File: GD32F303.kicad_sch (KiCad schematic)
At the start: 0 parts

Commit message: 更新原理图
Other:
- sheet MCU_Core ports: added CAN_RX, CAN_TX, RS232_RX, RS232_TX, RS485_DE, RS485_RX, RS485_TX, USB_DM, USB_DP; removed none
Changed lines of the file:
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@@
 	(paper "A3")
 	(sheet
-		(at 272.415 133.985)
-		(size 26.035 13.335)
+		(at 196.977 137.922)
+		(size 24.765 13.335)
 		(exclude_from_sim no)
 		(in_bom yes)
@@
 		)
 		(property "Sheetname" "RS485"
-			(at 272.415 133.2734 0)
+			(at 196.977 137.2104 0)
 			(show_name no)
 			(do_not_autoplace no)
@@
 		)
 		(property "Sheetfile" "RS485.kicad_sch"
-			(at 272.415 147.9046 0)
+			(at 196.977 151.8416 0)
 			(show_name no)
 			(do_not_autoplace no)
@@
 	)
 	(sheet
-		(at 273.05 90.805)
-		(size 28.575 15.875)
+		(at 197.612 96.012)
+		(size 24.13 14.605)
 		(exclude_from_sim no)
 		(in_bom yes)
@@
 		)
 		(property "Sheetname" "CAN"
-			(at 273.05 90.0934 0)
+			(at 197.612 95.3004 0)
 			(show_name no)
 			(do_not_autoplace no)
@@
 		)
 		(property "Sheetfile" "CAN.kicad_sch"
-			(at 273.05 107.2646 0)
+			(at 197.612 111.2016 0)
 			(show_name no)
 			(do_not_autoplace no)
@@
 	)
 	(sheet
-		(at 273.05 114.3)
+		(at 197.612 118.237)
 		(size 24.13 14.605)
 		(exclude_from_sim no)
@@
 		)
 		(property "Sheetname" "RS232"
-			(at 273.05 113.5884 0)
+			(at 197.612 117.5254 0)
 			(show_name no)
 			(do_not_autoplace no)
@@
 		)
 		(property "Sheetfile" "RS232.kicad_sch"
-			(at 273.05 129.4896 0)
+			(at 197.612 133.4266 0)
 			(show_name no)
 			(do_not_autoplace no)
@@
 	)
 	(sheet
-		(at 149.86 91.059)
-		(size 30.48 36.576)
+		(at 139.7 21.844)
+		(size 114.935 36.576)
 		(exclude_from_sim no)
 		(in_bom yes)
@@
 		)
 		(property "Sheetname" "POWER"
-			(at 149.86 90.3474 0)
+			(at 139.7 21.1324 0)
 			(show_name no)
 			(do_not_autoplace no)
@@
 		)
 		(property "Sheetfile" "POWER.kicad_sch"
-			(at 149.86 128.2196 0)
+			(at 139.7 59.0046 0)
 			(show_name no)
 			(do_not_autoplace no)
@@
 	)
 	(sheet
-		(at 203.708 90.043)
+		(at 128.27 93.98)
 		(size 35.306 53.086)
 		(exclude_from_sim no)
@@
 		)
 		(property "Sheetname" "MCU_Core"
-			(at 203.708 89.3314 0)
+			(at 128.27 93.2684 0)
 			(show_name no)
 			(do_not_autoplace no)
@@
 		)
 		(property "Sheetfile" "STM32F303VCT6.kicad_sch"
-			(at 203.708 143.7136 0)
-			(show_name no)
-			(do_not_autoplace no)
-			(effects
-				(font
-					(size 1.27 1.27)
-				)
-				(justify left top)
-			)
-		)
+			(at 128.27 147.6506 0)
+			(show_name no)
+			(do_not_autoplace no)
+			(effects
+				(font
+					(size 1.27 1.27)
+				)
+				(justify left top)
+			)
+		)
+		(pin "CAN_RX" input
+			(at 163.576 100.33 0)
+			(effects
+				(font
+					(size 1.27 1.27)
+				)
+				(justify right)
+			)
+		)
+		(pin "RS232_RX" input
+			(at 163.576 128.27 0)
+			(effects
+				(font
+					(size 1.27 1.27)
+				)
+				(justify right)
+			)
+		)
+		(pin "CAN_TX" output
+			(at 163.576 104.14 0)
+			(effects
+				(font
+					(size 1.27 1.27)
+				)
+				(justify right)
+			)
+		)
+		(pin "RS232_TX" output
+			(at 163.576 124.46 0)
+			(effects
+				(font
+					(size 1.27 1.27)
+				)
+				(justify right)
+			)
+		)
+		(pin "RS485_RX" bidirectional
+			(at 163.576 142.24 0)
+			(effects
+				(font
+					(size 1.27 1.27)
+				)
+				(justify right)
+			)
+		)
+		(pin "RS485_TX" bidirectional
+			(at 163.576 139.7 0)
+			(effects
+				(font
+					(size 1.27 1.27)
+				)
+				(justify right)
+			)
+		)
+		(pin "RS485_DE" output
+			(at 163.576 137.16 0)
+			(effects
+				(font
+					(size 1.27 1.27)
+				)
+				(justify right)
+			)
+		)
+		(pin "USB_DP" bidirectional
+			(at 128.27 107.95 180)
+			(effects
+				(font
+					(size 1.27 1.27)
+				)
+				(justify left)
+			)
+		)
+		(pin "USB_DM" bidirectional
+			(at 128.27 111.76 180)
+			(effects
+				(font
+					(size 1.27 1.27)
+				)
+				(justify left)
+			)
+		)

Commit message: 增加USB,TYPEC转串口esd隔离，
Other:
- sheet MCU_Core ports: added MCU_RS232_RX, MCU_RS232_TX; removed RS232_RX, RS232_TX
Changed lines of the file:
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@@
 			)
 		)
-		(pin "RS232_RX" input
+		(pin "MCU_RS232_RX" input
 			(at 163.576 128.27 0)
 			(effects
@@
 			)
 		)
-		(pin "RS232_TX" output
+		(pin "MCU_RS232_TX" output
 			(at 163.576 124.46 0)
 			(effects

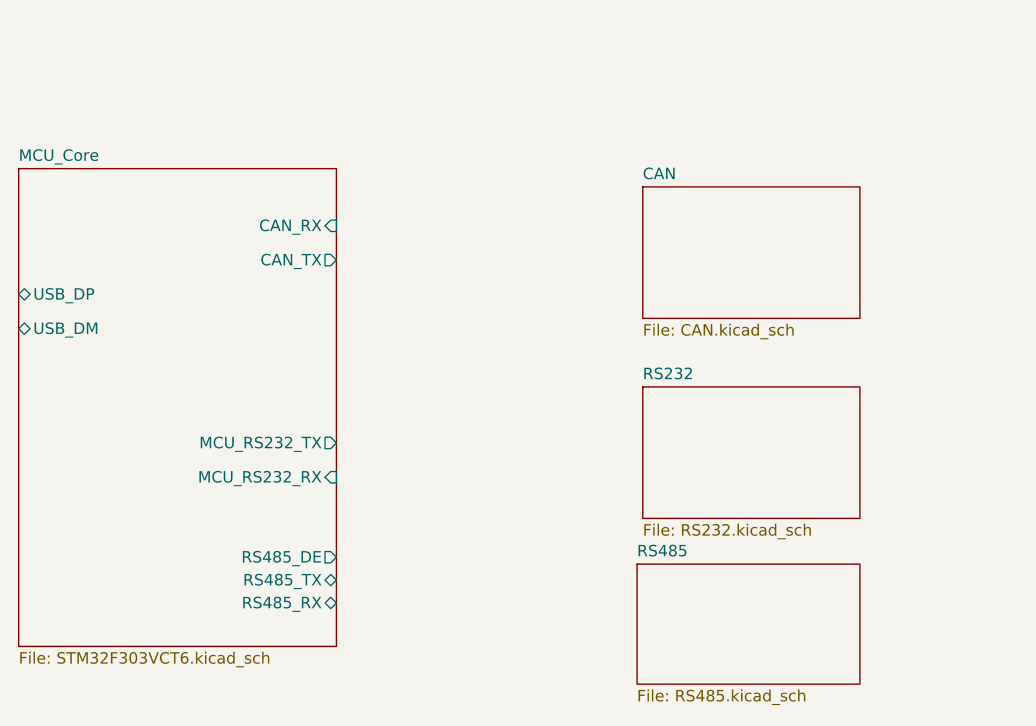
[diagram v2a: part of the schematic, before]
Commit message: 完成GD32F303控制板原理图与PCB设计
- 更新电源、CAN、RS232、RS485及电机通信子电路
- 切换并完善GD32F303VCT6核心原理图
- 新增PCB布局及所需符号、封装库文件
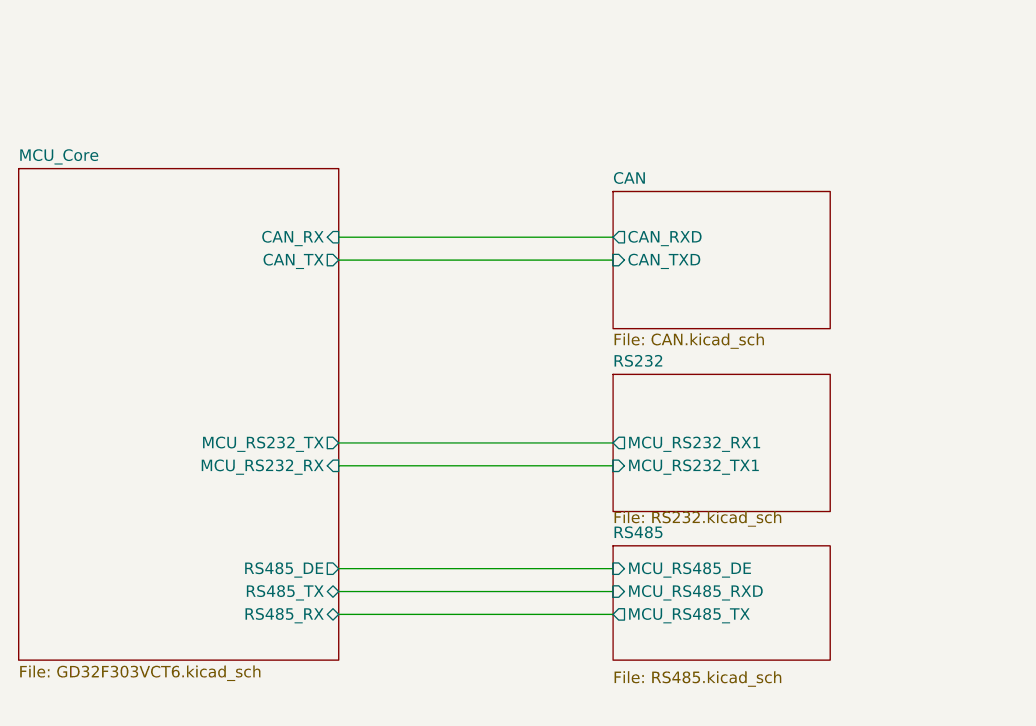
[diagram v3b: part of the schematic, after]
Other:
- sheet CAN ports: added CAN_RXD, CAN_TXD; removed none
- sheet MCU_Core: file STM32F303VCT6.kicad_sch -> GD32F303VCT6.kicad_sch
- sheet MCU_Core ports: added none; removed USB_DM, USB_DP
- sheet RS232 ports: added MCU_RS232_RX1, MCU_RS232_TX1; removed none
- sheet RS485 ports: added MCU_RS485_DE, MCU_RS485_RXD, MCU_RS485_TX; removed none
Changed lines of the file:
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@@
 	(generator_version "10.0")
 	(paper "A3")
+	(wire
+		(pts
+			(xy 163.83 143.51) (xy 194.31 143.51)
+		)
+		(stroke
+			(width 0)
+			(type default)
+		)
+	)
+	(wire
+		(pts
+			(xy 194.31 124.46) (xy 163.83 124.46)
+		)
+		(stroke
+			(width 0)
+			(type default)
+		)
+	)
+	(wire
+		(pts
+			(xy 163.83 127) (xy 194.31 127)
+		)
+		(stroke
+			(width 0)
+			(type default)
+		)
+	)
+	(wire
+		(pts
+			(xy 194.31 101.6) (xy 163.83 101.6)
+		)
+		(stroke
+			(width 0)
+			(type default)
+		)
+	)
+	(wire
+		(pts
+			(xy 163.83 140.97) (xy 194.31 140.97)
+		)
+		(stroke
+			(width 0)
+			(type default)
+		)
+	)
+	(wire
+		(pts
+			(xy 163.83 104.14) (xy 194.31 104.14)
+		)
+		(stroke
+			(width 0)
+			(type default)
+		)
+	)
+	(wire
+		(pts
+			(xy 163.83 138.43) (xy 194.31 138.43)
+		)
+		(stroke
+			(width 0)
+			(type default)
+		)
+	)
 	(sheet
-		(at 196.977 137.922)
-		(size 24.765 13.335)
+		(at 194.31 135.89)
+		(size 24.13 12.7)
 		(exclude_from_sim no)
 		(in_bom yes)
@@
 		)
 		(property "Sheetname" "RS485"
-			(at 196.977 137.2104 0)
+			(at 194.31 135.1784 0)
 			(show_name no)
 			(do_not_autoplace no)
@@
 		)
 		(property "Sheetfile" "RS485.kicad_sch"
-			(at 196.977 151.8416 0)
+			(at 194.31 149.8096 0)
 			(show_name no)
 			(do_not_autoplace no)
@@
 				)
 				(justify left top)
+			)
+		)
+		(pin "MCU_RS485_DE" input
+			(at 194.31 138.43 180)
+			(effects
+				(font
+					(size 1.27 1.27)
+				)
+				(justify left)
+			)
+		)
+		(pin "MCU_RS485_TX" output
+			(at 194.31 143.51 180)
+			(effects
+				(font
+					(size 1.27 1.27)
+				)
+				(justify left)
+			)
+		)
+		(pin "MCU_RS485_RXD" input
+			(at 194.31 140.97 180)
+			(effects
+				(font
+					(size 1.27 1.27)
+				)
+				(justify left)
 			)
 		)
@@
 	)
 	(sheet
-		(at 197.612 96.012)
-		(size 24.13 14.605)
+		(at 194.31 96.52)
+		(size 24.13 15.24)
+		(exclude_from_sim no)
+		(in_bom yes)
+		(on_board yes)
+		(dnp no)
+		(stroke
+			(width 0.1524)
+			(type solid)
+		)
+		(fill
+			(color 0 0 0 0)
+		)
+		(property "Sheetname" "CAN"
+			(at 194.31 95.8084 0)
+			(show_name no)
+			(do_not_autoplace no)
+			(effects
+				(font
+					(size 1.27 1.27)
+				)
+				(justify left bottom)
+			)
+		)
+		(property "Sheetfile" "CAN.kicad_sch"
+			(at 194.31 112.268 0)
+			(show_name no)
+			(do_not_autoplace no)
+			(effects
+				(font
+					(size 1.27 1.27)
+				)
+				(justify left top)
+			)
+		)
+		(pin "CAN_RXD" output
+			(at 194.31 101.6 180)
+			(effects
+				(font
+					(size 1.27 1.27)
+				)
+				(justify left)
+			)
+		)
+		(pin "CAN_TXD" input
+			(at 194.31 104.14 180)
+			(effects
+				(font
+					(size 1.27 1.27)
+				)
+				(justify left)
+			)
+		)
+		(instances
+			(project "GD32F303"
+				(path "/54005433-e3aa-4693-8f75-bb73943288d3"
+					(page "4")
+				)
+			)
+		)
+	)
+	(sheet
+		(at 194.31 116.84)
+		(size 24.13 15.24)
 		(exclude_from_sim no)
 		(in_bom yes)
@@
 			(color 0 0 0 0)
 		)
-		(property "Sheetname" "CAN"
-			(at 197.612 95.3004 0)
+		(property "Sheetname" "RS232"
+			(at 194.31 116.1284 0)
 			(show_name no)
 			(do_not_autoplace no)
@@
 			)
 		)
-		(property "Sheetfile" "CAN.kicad_sch"
-			(at 197.612 111.2016 0)
+		(property "Sheetfile" "RS232.kicad_sch"
+			(at 194.31 132.0296 0)
 			(show_name no)
 			(do_not_autoplace no)
@@
 			)
 		)
-		(instances
-			(project "GD32F303"
-				(path "/54005433-e3aa-4693-8f75-bb73943288d3"
-					(page "4")
-				)
-			)
-		)
-	)
-	(sheet
-		(at 197.612 118.237)
-		(size 24.13 14.605)
-		(exclude_from_sim no)
-		(in_bom yes)
-		(on_board yes)
-		(dnp no)
-		(fields_autoplaced yes)
-		(stroke
-			(width 0.1524)
-			(type solid)
-		)
-		(fill
-			(color 0 0 0 0)
-		)
-		(property "Sheetname" "RS232"
-			(at 197.612 117.5254 0)
-			(show_name no)
-			(do_not_autoplace no)
-			(effects
-				(font
-					(size 1.27 1.27)
-				)
-				(justify left bottom)
-			)
-		)
-		(property "Sheetfile" "RS232.kicad_sch"
-			(at 197.612 133.4266 0)
-			(show_name no)
-			(do_not_autoplace no)
-			(effects
-				(font
-					(size 1.27 1.27)
-				)
-				(justify left top)
+		(pin "MCU_RS232_TX1" input
+			(at 194.31 127 180)
+			(effects
+				(font
+					(size 1.27 1.27)
+				)
+				(justify left)
+			)
+		)
+		(pin "MCU_RS232_RX1" output
+			(at 194.31 124.46 180)
+			(effects
+				(font
+					(size 1.27 1.27)
+				)
+				(justify left)
 			)
 		)
@@
 	(sheet
 		(at 128.27 93.98)
-		(size 35.306 53.086)
+		(size 35.56 54.61)
 		(exclude_from_sim no)
 		(in_bom yes)
@@
 			)
 		)
-		(property "Sheetfile" "STM32F303VCT6.kicad_sch"
-			(at 128.27 147.6506 0)
+		(property "Sheetfile" "GD32F303VCT6.kicad_sch"
+			(at 128.27 149.1746 0)
 			(show_name no)
 			(do_not_autoplace no)
@@
 		)
 		(pin "CAN_RX" input
-			(at 163.576 100.33 0)
+			(at 163.83 101.6 0)
 			(effects
 				(font
@@
 		)
 		(pin "MCU_RS232_RX" input
-			(at 163.576 128.27 0)
+			(at 163.83 127 0)
 			(effects
 				(font
@@
 		)
 		(pin "CAN_TX" output
-			(at 163.576 104.14 0)
+			(at 163.83 104.14 0)
 			(effects
 				(font
@@
 		)
 		(pin "MCU_RS232_TX" output
-			(at 163.576 124.46 0)
+			(at 163.83 124.46 0)
 			(effects
 				(font
@@
 		)
 		(pin "RS485_RX" bidirectional
-			(at 163.576 142.24 0)
+			(at 163.83 143.51 0)
 			(effects
 				(font
@@
 		)
 		(pin "RS485_TX" bidirectional
-			(at 163.576 139.7 0)
+			(at 163.83 140.97 0)
 			(effects
 				(font
@@
 		)
 		(pin "RS485_DE" output
-			(at 163.576 137.16 0)
-			(effects
-				(font
-					(size 1.27 1.27)
-				)
-				(justify right)
-			)
-		)
-		(pin "USB_DP" bidirectional
-			(at 128.27 107.95 180)
-			(effects
-				(font
-					(size 1.27 1.27)
-				)
-				(justify left)
-			)
-		)
-		(pin "USB_DM" bidirectional
-			(at 128.27 111.76 180)
-			(effects
-				(font
-					(size 1.27 1.27)
-				)
-				(justify left)
-			)
-		)
+			(at 163.83 138.43 0)
+			(effects
+				(font
+					(size 1.27 1.27)
+				)
+				(justify right)
+			)
+		)
